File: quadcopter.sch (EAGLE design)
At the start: 69 parts, among them J4 AVR_SPI_PRG_6NS, M1 MOTOR_PADS, M2 MOTOR_PADS, M3 MOTOR_PADS, M4 MOTOR_PADS, U1 ATMEGA128RFA1

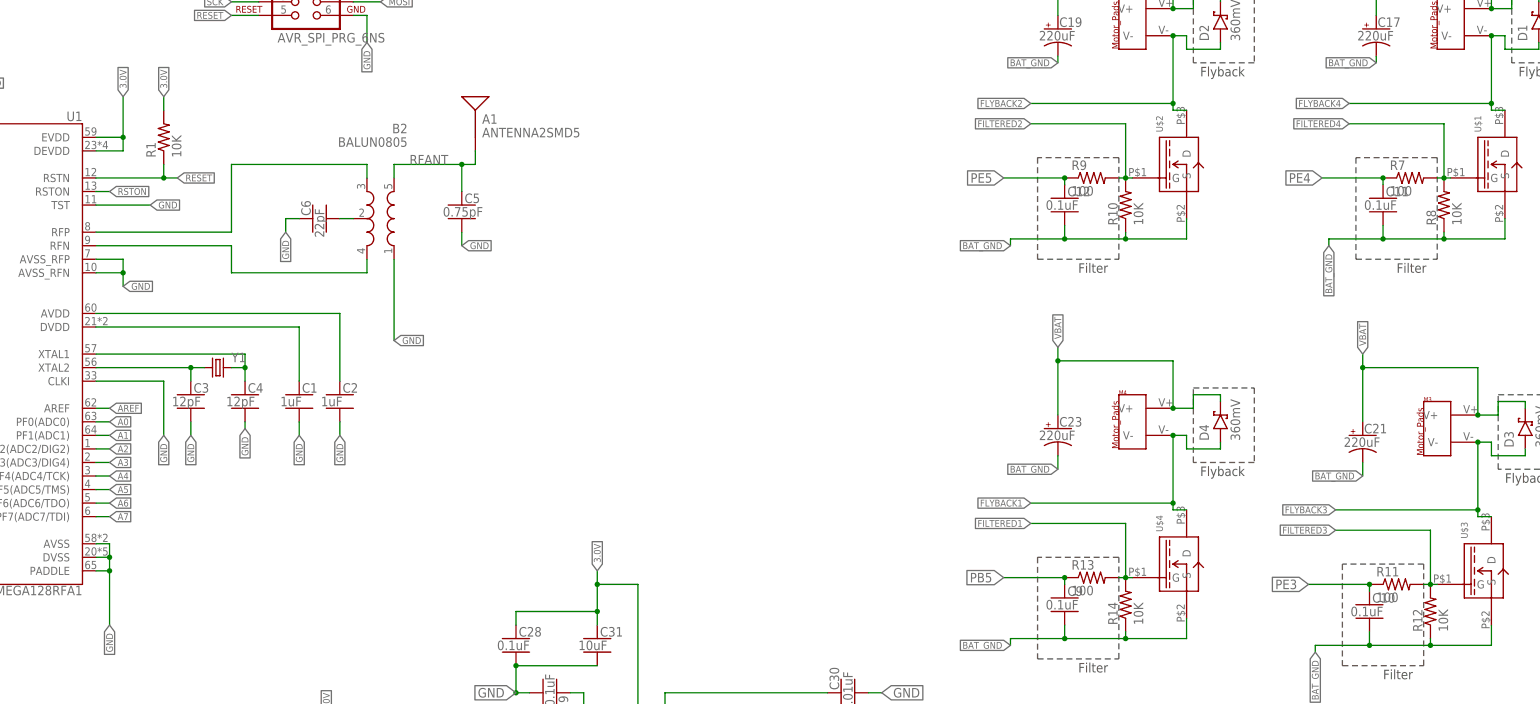
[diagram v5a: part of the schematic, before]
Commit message: Finish Board Layers (still need to route
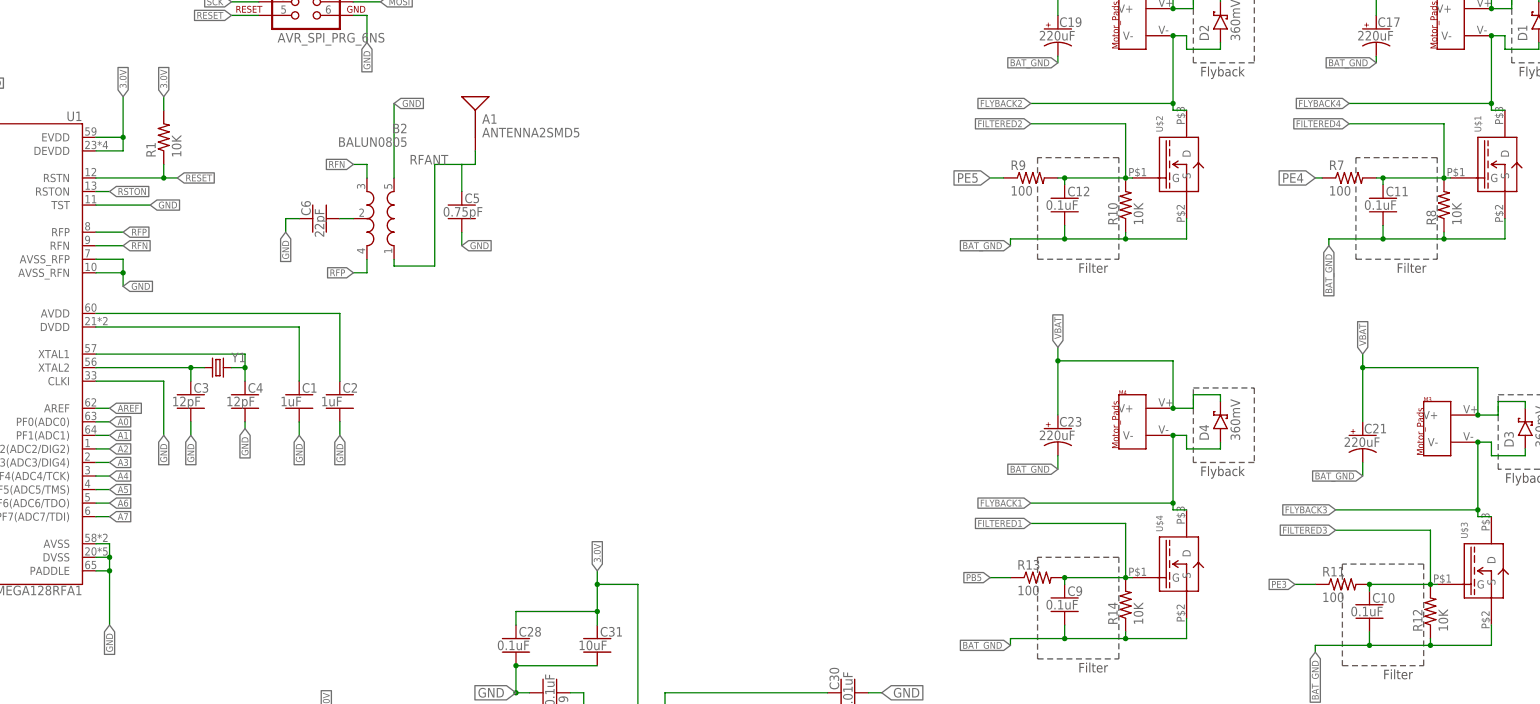
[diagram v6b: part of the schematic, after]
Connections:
- net FILTERED1: now also C9.1
- net FILTERED2: now also C12.1
- net FILTERED3: now also C10.1
- net FILTERED4: now also C11.1
- net GND: now also B2.GND@5; no longer B2.IN
- net PB5: no longer C9.1
- net PE3: no longer C10.1
- net PE4: no longer C11.1
- net PE5: no longer C12.1
- net RFANT: now also B2.IN; no longer B2.GND@5
- net RFN: now also B2.OUT2; no longer B2.OUT1
- net RFP: now also B2.OUT1; no longer B2.OUT2
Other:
- moved on the sheet: R11, R13, R7, R9

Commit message: Push Board
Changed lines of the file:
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@@
 <setting verticaltext="up"/>
 </settings>
-<grid distance="0.1" unitdist="inch" unit="inch" style="lines" multiple="1" display="no" altdistance="0.01" altunitdist="inch" altunit="inch"/>
+<grid distance="0.05" unitdist="inch" unit="inch" style="lines" multiple="1" display="no" altdistance="0.01" altunitdist="inch" altunit="inch"/>
 <layers>
 <layer number="1" name="Top" color="4" fill="1" visible="no" active="no"/>
@@
 <wire x1="152.4" y1="74.93" x2="144.78" y2="74.93" width="0.1524" layer="91"/>
 <wire x1="144.78" y1="74.93" x2="144.78" y2="76.2" width="0.1524" layer="91"/>
+<junction x="157.48" y="93.98"/>
 </segment>
 </net>
@@
 </segment>
 </net>
-<net name="PE3" class="2">
+<net name="PE3" class="0">
 <segment>
 <pinref part="U1" gate="G$1" pin="PE3(OC3A/AIN1)"/>
@@
 <net name="FILTERED1" class="2">
 <segment>
+<pinref part="R13" gate="G$1" pin="2"/>
+<pinref part="C9" gate="G$1" pin="1"/>
+<wire x1="270.51" y1="16.51" x2="270.51" y2="15.24" width="0.1524" layer="91"/>
 <wire x1="281.94" y1="26.67" x2="264.16" y2="26.67" width="0.1524" layer="91"/>
 <label x="264.16" y="26.67" size="1.27" layer="95" rot="R180" xref="yes"/>
@@
 <wire x1="281.94" y1="26.67" x2="281.94" y2="16.51" width="0.1524" layer="91"/>
 <junction x="281.94" y="16.51"/>
-<wire x1="280.67" y1="16.51" x2="281.94" y2="16.51" width="0.1524" layer="91"/>
 <pinref part="U$4" gate="G$1" pin="G"/>
 <wire x1="281.94" y1="16.51" x2="283.21" y2="16.51" width="0.1524" layer="91"/>
-</segment>
-<segment>
-<pinref part="R13" gate="G$1" pin="2"/>
-<wire x1="270.51" y1="16.51" x2="280.67" y2="16.51" width="0.1524" layer="91"/>
-<pinref part="C9" gate="G$1" pin="1"/>
-<wire x1="270.51" y1="16.51" x2="270.51" y2="15.24" width="0.1524" layer="91"/>
+<wire x1="270.51" y1="16.51" x2="281.94" y2="16.51" width="0.1524" layer="91"/>
 <junction x="270.51" y="16.51"/>
 </segment>
